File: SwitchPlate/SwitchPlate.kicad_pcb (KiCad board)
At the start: 2 copper layers, 429.5 x 133.3 mm, 10 parts

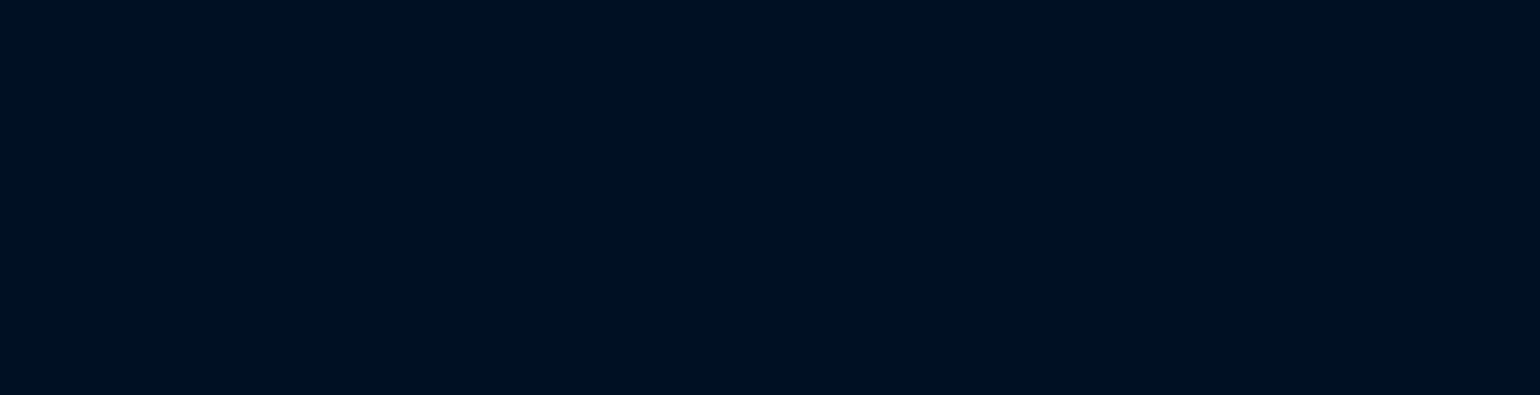
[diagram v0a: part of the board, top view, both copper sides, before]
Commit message: Added Logo and couple small corrections to traces.
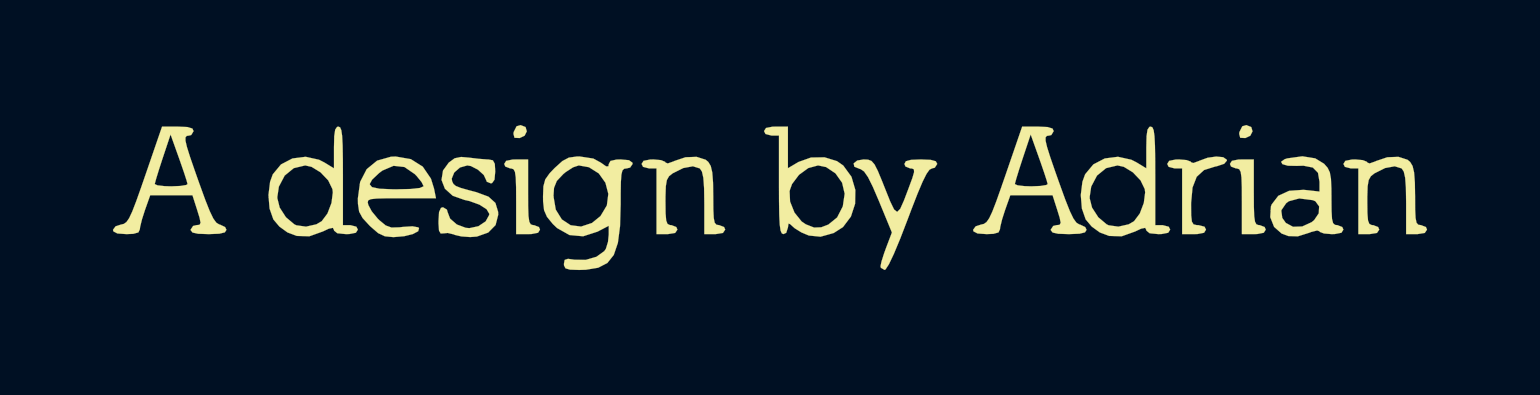
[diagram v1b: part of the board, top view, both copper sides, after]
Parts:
- added G***: LOGO, logo:logo, F.Cu at (458.9, 130.5)
